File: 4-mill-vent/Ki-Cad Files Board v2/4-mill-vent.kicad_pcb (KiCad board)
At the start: 2 copper layers, 76.2 x 47.6 mm, 74 parts, among them J1 Fan, J2 Buzzer, J3 Power, J4 ICSP, J9 Conn_01x02_Male, Q3 PZT3904, Q4 PZT3904, Q5 TSM480P06CP, Q6 MMBT3904, SW1 Power_off, SW2 Power_On, SW3 Fan_Down, SW4 Fan_Up, U1 LM321, U2 ATmega328P-AU, U3 TPSM84212EAB, U4 LM1117-5.0, U5 LM317_TO-220, Y1 16.000MHZ

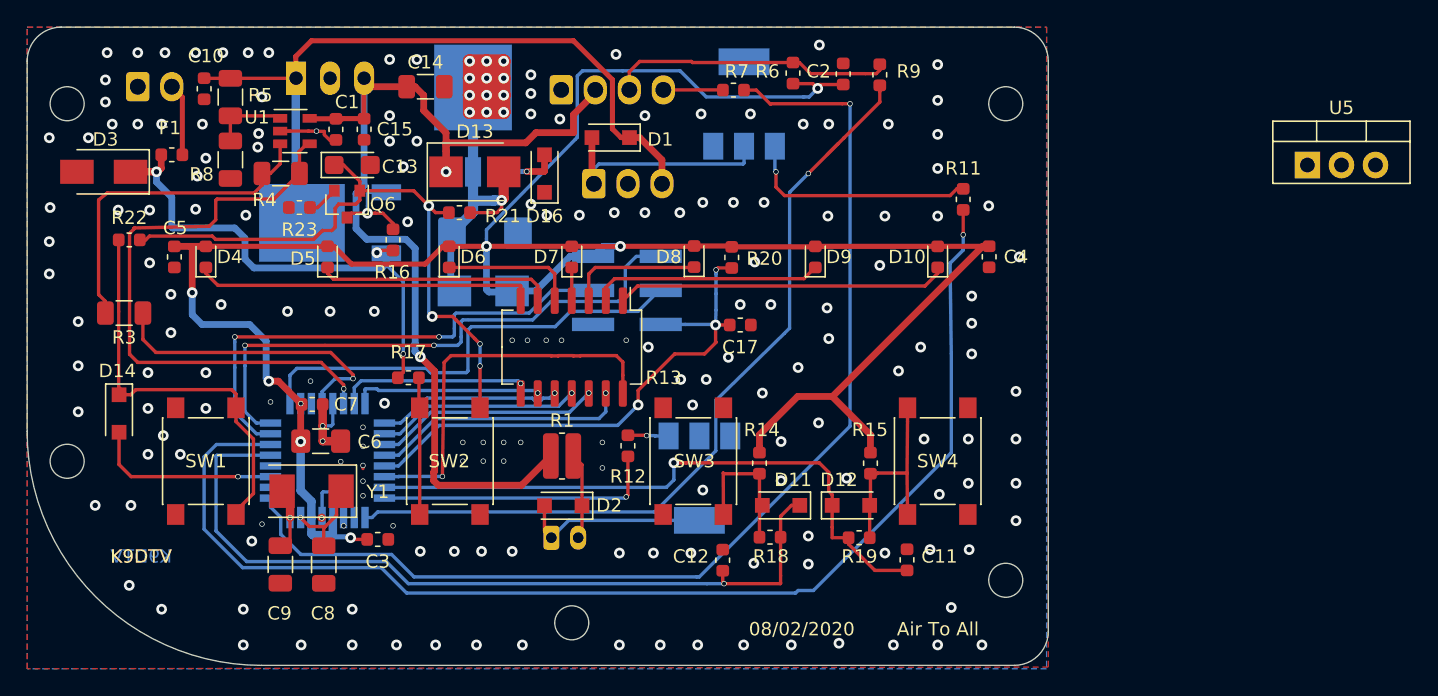
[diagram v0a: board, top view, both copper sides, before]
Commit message: Last Update USE V2
Board test complete, all slikscreen error are fixed in v2, Full use of opamp for battery monitoring.
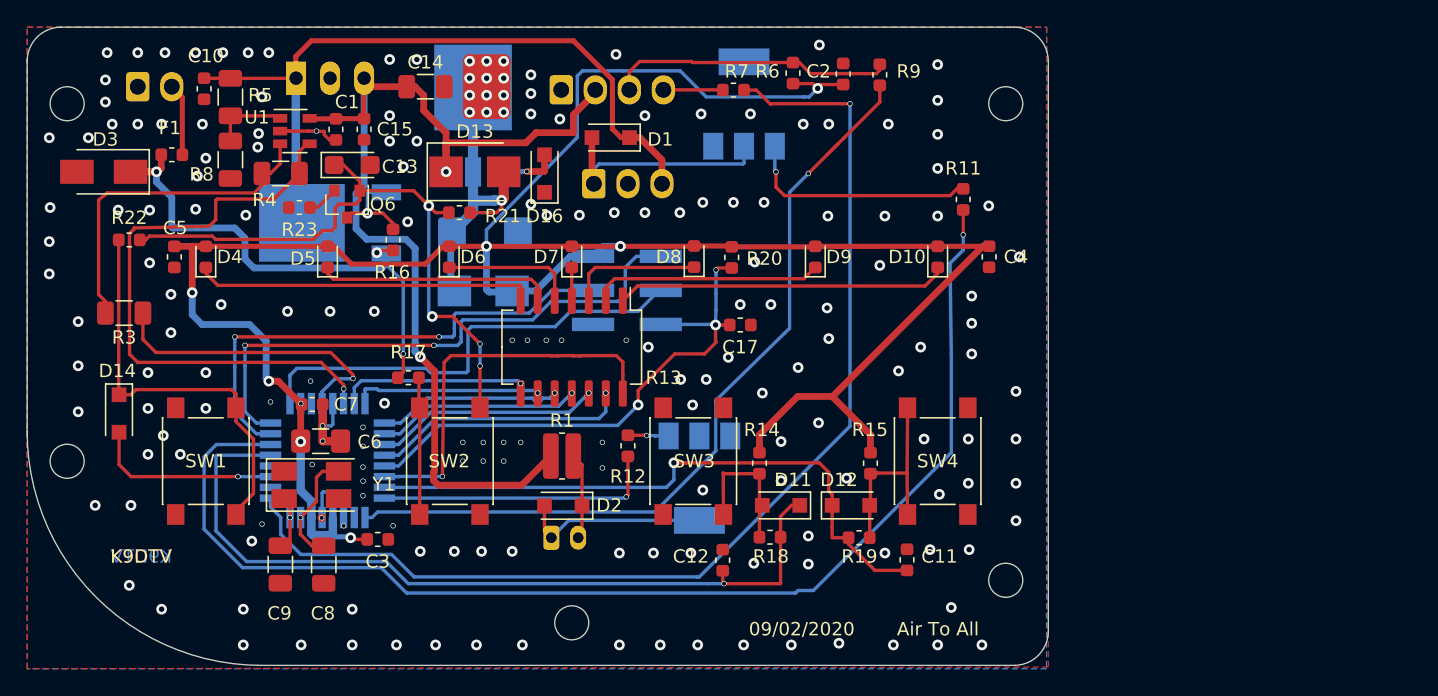
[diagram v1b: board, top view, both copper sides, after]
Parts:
- removed U5: LM317_TO-220, Package_TO_SOT_THT:TO-220-3_Vertical
- J9: value Conn_01x02_Male -> Mounting holes
- Y1: value 16.000MHZ -> Crystal_16MHz; footprint Crystal:Crystal_SMD_0603-2Pin_6.0x3.5mm -> Crystal:Crystal_SMD_0603-4Pin_6.0x3.5mm
- moved Y1 0.47 mm to (120.4, 102.5), turned to 0 degrees
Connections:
- Y1 pad 1: Net-(C8-Pad1) -> Net-(C9-Pad1)
- Y1 pad 2: Net-(C9-Pad1) -> GND
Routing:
- net Net-(C8-Pad1): track 7.88 -> 8.68 mm
- net Net-(C9-Pad1): track 4.39 -> 3.78 mm
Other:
- board text added: "09/02/2020"
- board text removed: "08/02/2020"
